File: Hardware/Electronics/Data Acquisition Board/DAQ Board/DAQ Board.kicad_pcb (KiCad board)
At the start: 4 copper layers, 105.4 x 58.9 mm, 142 parts, among them J1 Conn_01x01_Male, J10 ~CS~_TP, J11 Conn_01x01_Male, J12 START_TP, J13 Conn_01x01_Male, J14 MID_SUPPLY_TP, J15 AVDD_TP, J16 DVDD_TP, J17 Conn_01x01_Male, J18 Conn_01x01_Male, J19 Conn_01x01_Male, J2 USB_B_Mini, J3 Conn_01x01_Male, J4 DC Barrel Jack, J5 HC-05 BT Module, J6 ICSP Header, J7 VIN_RAW_TP, J8 Conn_01x01_Male, J9 Conn_01x01_Male, Q1 DMP2100U, SW10 SW_SPDT, SW11 SW_SPDT, SW2 SW_DIP_x02, SW3 SW_SPDT, SW4 SW_SPDT, SW5 SW_SPDT, SW6 SW_SPDT, SW7 SW_SPDT, SW8 SW_SPDT, SW9 SW_SPDT, U1 ATmega328P-AU, U2 MCP1755T-5002E_SOT223-5, U3 LM3480-3.3, U4 MCP1755T-5002E_SOT223-5, U5 FT232RL, Y1 16MHz

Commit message: Seems to have imported ok
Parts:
- removed SW2: SW_DIP_x02, Switches:DIP-Switch_01x02
- added C63: 100n, Capacitor_SMD:C_0603_1608Metric, F.Cu at (122.7, 59.6)
- added C64: 10n, Capacitor_SMD:C_0603_1608Metric, F.Cu at (119.7, 61.1)
- added C65: 10n, Capacitor_SMD:C_0603_1608Metric, F.Cu at (119.7, 59.6)
- added C66: 100n, Capacitor_SMD:C_0603_1608Metric, F.Cu at (122.7, 58.0)
- added R28: 100k, Resistor_SMD:R_0603_1608Metric, F.Cu at (119.7, 58.0)
- added R29: 100k, Resistor_SMD:R_0603_1608Metric, F.Cu at (129.1, 58.0)
- added U6: TXS0108EPWR, Package_SO:TSSOP-20_4.4x6.5mm_P0.65mm, F.Cu at (114.2, 60.9)
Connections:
- net /ADC1299/DVDD renamed /+3V3
- ADC1 pad 34: /ADC1299/MOSI -> /MOSI_3V3
- ADC1 pad 35: /~PWDN -> /~PWDN_3V3
- ADC1 pad 36: /~RESET -> /~RESET_3V3
- ADC1 pad 38: /START -> /START_3V3
- ADC1 pad 39: /~CS -> /~CS_3V3
- ADC1 pad 40: /ADC1299/SCLK -> /SCLK_3V3
- ADC1 pad 43: /ADC1299/MISO -> /MISO_3V3
- ADC1 pad 47: /~DRDY -> /~DRDY_3V3
- C60 pad 2: /~RESET -> /~RESET_5V
- C62 pad 1: /~RESET -> /~RESET_5V
- J10 pad 2: /~CS -> /~CS_3V3
- J12 pad 2: /START -> /START_3V3
- J6 pad 1: /ADC1299/MISO -> /MISO_5V
- J6 pad 3: /ADC1299/SCLK -> /SCLK_5V
- J6 pad 4: /ADC1299/MOSI -> /MOSI_5V
- J6 pad 5: /~RESET -> /~RESET_5V
- PB1 pad 3: /~RESET -> /~RESET_5V
- PB1 pad 4: /~RESET -> /~RESET_5V
- R16 pad 2: /~RESET -> /~RESET_5V
- R20 pad 1: Net-(R20-Pad1) -> /Arduino Nano/SS_TX
- R21 pad 2: Net-(R20-Pad1) -> /Arduino Nano/SS_TX
- R27 pad 2: /~CS -> /~CS_3V3
- U1 pad 1: Net-(U1-Pad1) -> Net-(R23-Pad2)
- U1 pad 10: /~DRDY -> /~DRDY_5V
- U1 pad 11: /START -> /START_5V
- U1 pad 12: Net-(R23-Pad2) -> /HC05_RX
- U1 pad 13: /~CS -> /Arduino Nano/SS_TX
- U1 pad 15: /ADC1299/MOSI -> /MOSI_5V
- U1 pad 16: /ADC1299/MISO -> /MISO_5V
- U1 pad 17: /ADC1299/SCLK -> /SCLK_5V
- U1 pad 2: Net-(U1-Pad2) -> /~CS_5V
- U1 pad 29: /~RESET -> /~RESET_5V
- U1 pad 9: /~PWDN -> /~PWDN_5V
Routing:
- net /~CS: track 59.8 -> 0.00 mm, vias 3 -> 0
- net /~RESET: track 105.1 -> 55.2 mm, vias 3 -> 1
- net /~RESET_5V: track 0.00 -> 49.3 mm, vias 0 -> 2
- net /~CS_3V3: track 0.00 -> 40.9 mm, vias 0 -> 2
- net /~PWDN: track 37.5 -> 0.00 mm, vias 2 -> 0
- net Net-(R23-Pad2): track 32.7 -> 0.00 mm
- net /~PWDN_3V3: track 0.00 -> 26.9 mm, vias 0 -> 1
- net /ADC1299/MISO: track 26.5 -> 0.00 mm, vias 1 -> 0
- net /HC05_RX: track 14.4 -> 0.00 mm
- net /MISO_5V: track 0.00 -> 12.7 mm
- net /Arduino Nano/RX: track 24.3 -> 15.0 mm
- net /Arduino Nano/TX: track 18.5 -> 13.0 mm
- net Net-(R20-Pad1): track 5.14 -> 0.00 mm
- net /Arduino Nano/SS_TX: track 0.00 -> 5.14 mm
- net /~PWDN_5V: track 0.00 -> 3.74 mm
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
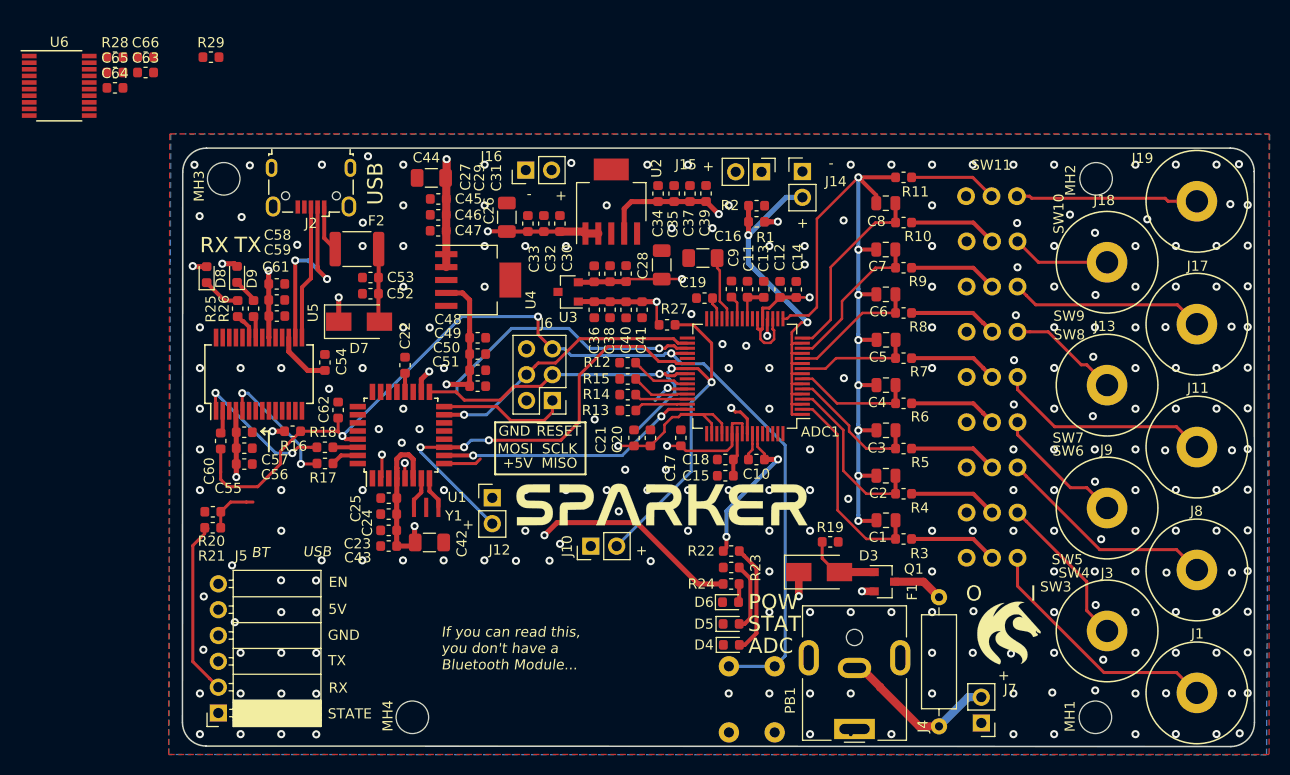
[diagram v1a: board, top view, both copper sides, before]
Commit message: Wired up level shifter and made changes to ADS1299 schematic to match breakout board
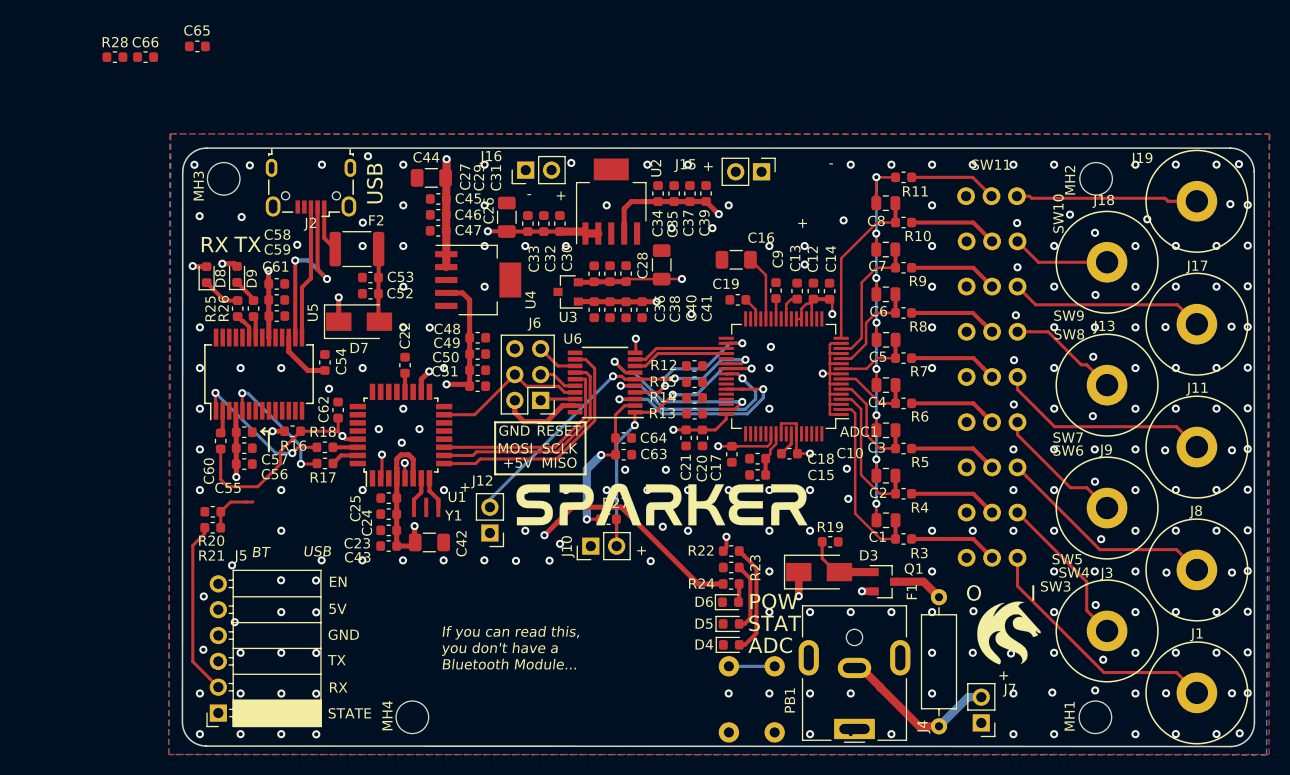
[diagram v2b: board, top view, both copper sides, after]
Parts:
- removed C11: 0.1uF, Capacitor_SMD:C_0603_1608Metric
- removed J14: MID_SUPPLY_TP, Connector_PinHeader_2.54mm:PinHeader_1x02_P2.54mm_Vertical
- removed R1, R2: 10k, Resistor_SMD:R_0603_1608Metric
- removed R29: 100k, Resistor_SMD:R_0603_1608Metric
- C13: value 1uF -> 10uF
- moved U6 61.1 mm to (167.9, 90.0), turned to 180 degrees
- moved C64 60.7 mm to (169.7, 95.5)
- moved C63 60.2 mm to (169.7, 97.1)
- moved R27 20.0 mm to (168.2, 103.5)
- moved C65 8.50 mm to (127.8, 57.0), turned to 180 degrees
- moved R12 6.58 mm to (176.7, 88.4)
- moved R15 6.58 mm to (176.7, 90.0)
- moved R13 6.58 mm to (176.7, 93.1)
- moved R14 6.58 mm to (176.7, 91.6)
- moved C17 5.27 mm to (180.3, 97.1), turned to 90 degrees
- moved C20 5.12 mm to (177.4, 95.5), turned to 270 degrees
- moved C21 5.12 mm to (175.8, 95.5), turned to 270 degrees
- moved C9 4.38 mm to (184.7, 81.0)
- moved ADC1 3.83 mm to (185.4, 89.4)
- moved J12 3.47 mm to (156.5, 104.8), turned to 180 degrees
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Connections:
- ADC1 pad 1: /ADC1299/MID_SUPPLY -> /ADC1299/AVDD
- ADC1 pad 11: /ADC1299/MID_SUPPLY -> /ADC1299/AVDD
- ADC1 pad 13: /ADC1299/MID_SUPPLY -> /ADC1299/AVDD
- ADC1 pad 15: /ADC1299/MID_SUPPLY -> /ADC1299/AVDD
- ADC1 pad 3: /ADC1299/MID_SUPPLY -> /ADC1299/AVDD
- ADC1 pad 5: /ADC1299/MID_SUPPLY -> /ADC1299/AVDD
- ADC1 pad 58: Net-(ADC1-Pad58) -> /GND
- ADC1 pad 7: /ADC1299/MID_SUPPLY -> /ADC1299/AVDD
- ADC1 pad 9: /ADC1299/MID_SUPPLY -> /ADC1299/AVDD
- C10 pad 2: Net-(ADC1-Pad58) -> /GND
- C13 pad 1: Net-(ADC1-Pad24) -> /GND
- C13 pad 2: /GND -> Net-(ADC1-Pad24)
- U6 pad 17: /MISO_5V -> /MOSI_5V
- U6 pad 18: /MOSI_5V -> /MISO_5V
- U6 pad 3: /MOSI_3V3 -> /MISO_3V3
- U6 pad 4: /MISO_3V3 -> /MOSI_3V3
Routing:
- net /~RESET: track 55.2 -> 0.00 mm, vias 1 -> 0
- net /START: track 44.2 -> 0.00 mm, vias 3 -> 0
- net /ADC1299/MID_SUPPLY: track 39.1 -> 0.00 mm, vias 2 -> 0
- net /START_3V3: track 0.00 -> 33.9 mm, vias 0 -> 3
- net /ADC1299/MOSI: track 27.2 -> 0.00 mm, vias 1 -> 0
- net /ADC1299/SCLK: track 26.9 -> 0.00 mm, vias 1 -> 0
- net /~DRDY: track 25.8 -> 0.00 mm, vias 2 -> 0
- net Net-(ADC1-Pad17): track 71.5 -> 48.6 mm
- net /~DRDY_5V: track 0.00 -> 21.6 mm
- net /SCLK_3V3: track 0.00 -> 20.4 mm, vias 0 -> 2
- net /~PWDN_5V: track 3.74 -> 24.0 mm
- net /START_5V: track 0.00 -> 19.9 mm
- net /~RESET_5V: track 49.3 -> 30.0 mm, vias 2 -> 1
- net /~DRDY_3V3: track 0.00 -> 18.5 mm, vias 0 -> 2
- net /MISO_3V3: track 3.73 -> 21.4 mm, vias 1 -> 2
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
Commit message: All traces routed
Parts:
- moved R28 56.3 mm to (168.8, 85.6), turned to 180 degrees
- moved C66 53.4 mm to (161.0, 95.3), turned to 270 degrees
- moved C65 51.7 mm to (162.6, 95.3), turned to 270 degrees
- moved D5 40.0 mm to (141.2, 105.4), turned to 90 degrees
- moved R23 39.6 mm to (141.1, 102.2), turned to 90 degrees
- moved C17 2.48 mm to (182.5, 98.3)
- moved D4 2.46 mm to (180.2, 113.4)
- moved C18 2.08 mm to (184.9, 97.6), turned to 180 degrees
- moved C15 2.08 mm to (184.9, 99.1), turned to 180 degrees
- moved C10 1.92 mm to (187.8, 97.8), turned to 270 degrees
- moved R22 1.60 mm to (180.2, 108.2)
- moved C48 1.20 mm to (155.4, 84.4)
- moved C49 1.20 mm to (155.4, 86.0)
- moved C51 1.20 mm to (155.4, 89.2)
- moved C50 1.20 mm to (155.4, 87.6)
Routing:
- net /~RESET_5V: track 30.0 -> 106.2 mm
- net /HC05_RX: track 0.00 -> 34.4 mm, vias 0 -> 1
- net /Arduino Nano/SS_TX: track 5.14 -> 26.8 mm, vias 0 -> 2
- net /~CS_5V: track 2.39 -> 23.7 mm, vias 1 -> 2
- net Net-(ADC1-Pad17): track 48.6 -> 63.3 mm
- net /+3V3: track 75.1 -> 88.5 mm, vias 5 -> 6
- net /SCLK_5V: track 3.85 -> 16.4 mm
- net /MISO_5V: track 3.45 -> 15.1 mm, vias 0 -> 1
- net /ADC1299/AVDD: track 61.8 -> 70.9 mm
- net Net-(D5-Pad2): track 6.77 -> 1.58 mm
- net Net-(R23-Pad2): track 0.00 -> 4.99 mm
- net Net-(D4-Pad2): track 10.9 -> 6.26 mm
- net /START_3V3: track 33.9 -> 38.2 mm
- net Net-(ADC1-Pad42): track 0.00 -> 3.84 mm
- net Net-(ADC1-Pad46): track 0.00 -> 3.00 mm
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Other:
- board text removed: "BT"

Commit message: Small schematic updates, changed test point nets, pcb changes
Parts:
- J15: value AVDD_TP -> VCAP1_TP
- J16: value DVDD_TP -> DRDY_TP
- moved J4 11.0 mm to (192.5, 113.1), turned to 0 degrees
- moved PB1 7.18 mm to (180.1, 123.6), turned to 90 degrees
- moved J15 2.72 mm to (180.5, 69.1), turned to 90 degrees
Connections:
- ADC1 pad 28: Net-(ADC1-Pad28) -> /ADC1299/VCAP1
- C16 pad 1: Net-(ADC1-Pad28) -> /ADC1299/VCAP1
- J15 pad 1: /GND -> /ADC1299/VCAP1
- J15 pad 2: /ADC1299/AVDD -> /GND
- J16 pad 2: /+3V3 -> /~DRDY_3V3
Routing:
- net /~DRDY_3V3: track 18.5 -> 39.9 mm
- net /+3V3: track 88.5 -> 68.5 mm
- net /ADC1299/VCAP1: track 0.00 -> 16.0 mm
- net Net-(ADC1-Pad28): track 6.45 -> 0.00 mm
- net /~RESET_5V: track 106.2 -> 108.9 mm
- net /VIN_RAW: track 16.1 -> 15.5 mm
- net /GND: vias 226 -> 252

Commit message: BLOCK B FAB
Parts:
- added J14: VREFP_TP, Connector_PinHeader_2.54mm:PinHeader_1x02_P2.54mm_Vertical, F.Cu at (187.4, 69.1)
- added LOGO3: VersionLogo, Sparker:Block2, F.Cu at (178.2, 105.7)
- moved R27 8.28 mm to (172.2, 96.2), turned to 90 degrees
- moved C58 3.18 mm to (135.6, 83.5)
- moved C61 3.10 mm to (135.6, 80.4)
- moved J10 2.06 mm to (164.4, 106.0)
- moved C59 0.06 mm to (135.6, 82.0)
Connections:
- net Net-(ADC1-Pad24) renamed /ADC1299/VREFP
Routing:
- net /ADC1299/VREFP: track 2.76 -> 17.7 mm
- net Net-(J2-Pad2): track 18.9 -> 13.9 mm
- net /+3V3: track 68.5 -> 63.5 mm, vias 6 -> 5
- net /GND: vias 252 -> 243
